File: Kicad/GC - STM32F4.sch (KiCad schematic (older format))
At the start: 16 parts, among them J2 SWD, U1 STM32F405RGT6, Y2 8MHz

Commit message: Passives changed from 0805 to 0603
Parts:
- C10, C11, C12, C13, C14, C15, C16, C17, C18, C19, C20, C9: footprint Capacitors_SMD:C_0805 -> Capacitors_SMD:C_0603
- R6: footprint Resistors_SMD:R_0805 -> Resistors_SMD:R_0603
- renumbered J2 to J9
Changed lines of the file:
@@
 F 0 "C11" H 7350 6300 50  0000 L CNN
 F 1 "2.2uF" H 7350 6100 50  0000 L CNN
-F 2 "Capacitors_SMD:C_0805" H 7300 6200 60  0001 C CNN
+F 2 "Capacitors_SMD:C_0603" H 7300 6200 60  0001 C CNN
 F 3 "" H 7300 6200 60  0001 C CNN
 	1    7300 6200
@@
 F 0 "C10" H 7350 6050 50  0000 L CNN
 F 1 "2.2uF" H 7350 5850 50  0000 L CNN
-F 2 "Capacitors_SMD:C_0805" H 7300 5950 60  0001 C CNN
+F 2 "Capacitors_SMD:C_0603" H 7300 5950 60  0001 C CNN
 F 3 "" H 7300 5950 60  0001 C CNN
 	1    7300 5950
@@
 F 0 "C9" H 7850 1800 50  0000 L CNN
 F 1 "15pF" H 8050 1800 50  0000 L CNN
-F 2 "Capacitors_SMD:C_0805" H 8000 1700 60  0001 C CNN
+F 2 "Capacitors_SMD:C_0603" H 8000 1700 60  0001 C CNN
 F 3 "" H 8000 1700 60  0001 C CNN
 	1    8000 1700
@@
 F 0 "C15" H 7800 1900 50  0000 L CNN
 F 1 "15pF" H 8050 1900 50  0000 L CNN
-F 2 "Capacitors_SMD:C_0805" H 8000 2000 60  0001 C CNN
+F 2 "Capacitors_SMD:C_0603" H 8000 2000 60  0001 C CNN
 F 3 "" H 8000 2000 60  0001 C CNN
 	1    8000 2000
@@
 F 0 "C12" H 7550 5650 50  0000 L CNN
 F 1 "2.2uF" H 7550 5450 50  0000 L CNN
-F 2 "Capacitors_SMD:C_0805" H 7500 5550 60  0001 C CNN
+F 2 "Capacitors_SMD:C_0603" H 7500 5550 60  0001 C CNN
 F 3 "" H 7500 5550 60  0001 C CNN
 	1    7500 5550
@@
 F 0 "C14" H 7800 5650 50  0000 L CNN
 F 1 "2.2uF" H 7800 5450 50  0000 L CNN
-F 2 "Capacitors_SMD:C_0805" H 7750 5550 60  0001 C CNN
+F 2 "Capacitors_SMD:C_0603" H 7750 5550 60  0001 C CNN
 F 3 "" H 7750 5550 60  0001 C CNN
 	1    7750 5550
@@
 F 0 "C13" H 7800 3050 50  0000 L CNN
 F 1 "100nF" H 7800 2850 50  0000 L CNN
-F 2 "Capacitors_SMD:C_0805" H 7750 2950 60  0001 C CNN
+F 2 "Capacitors_SMD:C_0603" H 7750 2950 60  0001 C CNN
 F 3 "" H 7750 2950 60  0001 C CNN
 	1    7750 2950
@@
 F 0 "C16" H 9450 1400 50  0000 L CNN
 F 1 "2.2uF" H 9450 1200 50  0000 L CNN
-F 2 "Capacitors_SMD:C_0805" H 9400 1300 60  0001 C CNN
+F 2 "Capacitors_SMD:C_0603" H 9400 1300 60  0001 C CNN
 F 3 "" H 9400 1300 60  0001 C CNN
 	1    9400 1300
@@
 F 0 "C17" H 9700 1400 50  0000 L CNN
 F 1 "2.2uF" H 9700 1200 50  0000 L CNN
-F 2 "Capacitors_SMD:C_0805" H 9650 1300 60  0001 C CNN
+F 2 "Capacitors_SMD:C_0603" H 9650 1300 60  0001 C CNN
 F 3 "" H 9650 1300 60  0001 C CNN
 	1    9650 1300
@@
 F 0 "C20" H 10450 1400 50  0000 L CNN
 F 1 "2.2uF" H 10450 1200 50  0000 L CNN
-F 2 "Capacitors_SMD:C_0805" H 10400 1300 60  0001 C CNN
+F 2 "Capacitors_SMD:C_0603" H 10400 1300 60  0001 C CNN
 F 3 "" H 10400 1300 60  0001 C CNN
 	1    10400 1300
@@
 F 0 "C18" H 9950 1400 50  0000 L CNN
 F 1 "2.2uF" H 9950 1200 50  0000 L CNN
-F 2 "Capacitors_SMD:C_0805" H 9900 1300 60  0001 C CNN
+F 2 "Capacitors_SMD:C_0603" H 9900 1300 60  0001 C CNN
 F 3 "" H 9900 1300 60  0001 C CNN
 	1    9900 1300
@@
 F 0 "C19" H 10200 1400 50  0000 L CNN
 F 1 "2.2uF" H 10200 1200 50  0000 L CNN
-F 2 "Capacitors_SMD:C_0805" H 10150 1300 60  0001 C CNN
+F 2 "Capacitors_SMD:C_0603" H 10150 1300 60  0001 C CNN
 F 3 "" H 10150 1300 60  0001 C CNN
 	1    10150 1300
@@
 	10150 1050 10400 1050
 $Comp
-L conn:Conn_02x03_Odd_Even J2
+L conn:Conn_02x03_Odd_Even J9
 U 1 1 53F77410
 P 9750 3050
-F 0 "J2" H 9800 3250 50  0000 C CNN
+F 0 "J9" H 9800 3250 50  0000 C CNN
 F 1 "SWD" H 9800 2850 50  0000 C CNN
 F 2 "Connectors:Tag-Connect_TC2030-IDC-NL" H 9750 3050 50  0001 C CNN
@@
 F 0 "R6" V 7350 2350 50  0000 C CNN
 F 1 "10k" V 7250 2350 50  0000 C CNN
-F 2 "Resistors_SMD:R_0805" V 7180 2350 50  0001 C CNN
+F 2 "Resistors_SMD:R_0603" V 7180 2350 50  0001 C CNN
 F 3 "" H 7250 2350 50  0001 C CNN
 	1    7250 2350

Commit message: Components placed
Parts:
- C12, C14, C16, C17, C18, C19, C20: value 2.2uF -> 100nF
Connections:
- net LAMP_CMD: now reaches U1.11 (PC3(ADC123_IN13))
- no-connect marks 9 -> 8
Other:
- moved on the sheet: C17, C18, C19, C20
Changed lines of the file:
@@
 $EndComp
 $Comp
-L Device:C C11
-U 1 1 53F757AE
-P 7300 6200
-AR Path="/53F757AE" Ref="C11"  Part="1"
-AR Path="/53F7501A/53F757AE" Ref="C11"  Part="1"
-F 0 "C11" H 7350 6300 50  0000 L CNN
-F 1 "2.2uF" H 7350 6100 50  0000 L CNN
-F 2 "Capacitors_SMD:C_0603" H 7300 6200 60  0001 C CNN
-F 3 "" H 7300 6200 60  0001 C CNN
-	1    7300 6200
-	0    -1   1    0
-$EndComp
-$Comp
-L Device:C C10
-U 1 1 53F757B5
-P 7300 5950
-AR Path="/53F757B5" Ref="C10"  Part="1"
-AR Path="/53F7501A/53F757B5" Ref="C10"  Part="1"
-F 0 "C10" H 7350 6050 50  0000 L CNN
-F 1 "2.2uF" H 7350 5850 50  0000 L CNN
-F 2 "Capacitors_SMD:C_0603" H 7300 5950 60  0001 C CNN
-F 3 "" H 7300 5950 60  0001 C CNN
-	1    7300 5950
-	0    -1   -1   0
-$EndComp
-$Comp
 L Device:C C9
 U 1 1 53F757DB
@@
 AR Path="/53F7501A/53F757F8" Ref="C12"  Part="1"
 F 0 "C12" H 7550 5650 50  0000 L CNN
-F 1 "2.2uF" H 7550 5450 50  0000 L CNN
+F 1 "100nF" H 7550 5450 50  0000 L CNN
 F 2 "Capacitors_SMD:C_0603" H 7500 5550 60  0001 C CNN
 F 3 "" H 7500 5550 60  0001 C CNN
@@
 AR Path="/53F7501A/53F757FF" Ref="C14"  Part="1"
 F 0 "C14" H 7800 5650 50  0000 L CNN
-F 1 "2.2uF" H 7800 5450 50  0000 L CNN
+F 1 "100nF" H 7800 5450 50  0000 L CNN
 F 2 "Capacitors_SMD:C_0603" H 7750 5550 60  0001 C CNN
 F 3 "" H 7750 5550 60  0001 C CNN
@@
 $EndComp
 NoConn ~ 7000 3300
-NoConn ~ 4500 4850
 Text GLabel 10050 3050 2    60   Input ~ 0
 SWCLK
@@
 AR Path="/53F7501A/53F77426" Ref="C16"  Part="1"
 F 0 "C16" H 9450 1400 50  0000 L CNN
-F 1 "2.2uF" H 9450 1200 50  0000 L CNN
+F 1 "100nF" H 9450 1200 50  0000 L CNN
 F 2 "Capacitors_SMD:C_0603" H 9400 1300 60  0001 C CNN
 F 3 "" H 9400 1300 60  0001 C CNN
@@
 L Device:C C17
 U 1 1 53F7742D
-P 9650 1300
+P 9700 1300
 AR Path="/53F7742D" Ref="C17"  Part="1"
 AR Path="/53F7501A/53F7742D" Ref="C17"  Part="1"
-F 0 "C17" H 9700 1400 50  0000 L CNN
-F 1 "2.2uF" H 9700 1200 50  0000 L CNN
-F 2 "Capacitors_SMD:C_0603" H 9650 1300 60  0001 C CNN
-F 3 "" H 9650 1300 60  0001 C CNN
-	1    9650 1300
+F 0 "C17" H 9750 1400 50  0000 L CNN
+F 1 "100nF" H 9750 1200 50  0000 L CNN
+F 2 "Capacitors_SMD:C_0603" H 9700 1300 60  0001 C CNN
+F 3 "" H 9700 1300 60  0001 C CNN
+	1    9700 1300
 	-1   0    0    1
 $EndComp
@@
 L Device:C C20
 U 1 1 53F77434
-P 10400 1300
+P 10650 1300
 AR Path="/53F77434" Ref="C20"  Part="1"
 AR Path="/53F7501A/53F77434" Ref="C20"  Part="1"
-F 0 "C20" H 10450 1400 50  0000 L CNN
-F 1 "2.2uF" H 10450 1200 50  0000 L CNN
-F 2 "Capacitors_SMD:C_0603" H 10400 1300 60  0001 C CNN
-F 3 "" H 10400 1300 60  0001 C CNN
-	1    10400 1300
+F 0 "C20" H 10700 1400 50  0000 L CNN
+F 1 "100nF" H 10700 1200 50  0000 L CNN
+F 2 "Capacitors_SMD:C_0603" H 10650 1300 60  0001 C CNN
+F 3 "" H 10650 1300 60  0001 C CNN
+	1    10650 1300
 	-1   0    0    1
 $EndComp
@@
 L Device:C C18
 U 1 1 53F77447
-P 9900 1300
+P 10000 1300
 AR Path="/53F77447" Ref="C18"  Part="1"
 AR Path="/53F7501A/53F77447" Ref="C18"  Part="1"
-F 0 "C18" H 9950 1400 50  0000 L CNN
-F 1 "2.2uF" H 9950 1200 50  0000 L CNN
-F 2 "Capacitors_SMD:C_0603" H 9900 1300 60  0001 C CNN
-F 3 "" H 9900 1300 60  0001 C CNN
-	1    9900 1300
+F 0 "C18" H 10050 1400 50  0000 L CNN
+F 1 "100nF" H 10050 1200 50  0000 L CNN
+F 2 "Capacitors_SMD:C_0603" H 10000 1300 60  0001 C CNN
+F 3 "" H 10000 1300 60  0001 C CNN
+	1    10000 1300
 	-1   0    0    1
 $EndComp
@@
 L Device:C C19
 U 1 1 53F7744E
-P 10150 1300
+P 10350 1300
 AR Path="/53F7744E" Ref="C19"  Part="1"
 AR Path="/53F7501A/53F7744E" Ref="C19"  Part="1"
-F 0 "C19" H 10200 1400 50  0000 L CNN
-F 1 "2.2uF" H 10200 1200 50  0000 L CNN
-F 2 "Capacitors_SMD:C_0603" H 10150 1300 60  0001 C CNN
-F 3 "" H 10150 1300 60  0001 C CNN
-	1    10150 1300
+F 0 "C19" H 10400 1400 50  0000 L CNN
+F 1 "100nF" H 10400 1200 50  0000 L CNN
+F 2 "Capacitors_SMD:C_0603" H 10350 1300 60  0001 C CNN
+F 3 "" H 10350 1300 60  0001 C CNN
+	1    10350 1300
 	-1   0    0    1
 $EndComp
-Connection ~ 10150 1550
 Wire Wire Line
-	10150 1550 10150 1450
-Connection ~ 9900 1550
+	10350 1550 10350 1450
 Wire Wire Line
-	9900 1550 9900 1450
-Connection ~ 9650 1550
+	10000 1550 10000 1450
 Wire Wire Line
-	9650 1550 9650 1450
-Connection ~ 9400 1550
+	9700 1550 9700 1450
 Wire Wire Line
 	9400 1450 9400 1550
-Connection ~ 9400 1050
 Wire Wire Line
 	9400 1050 9400 1150
-Connection ~ 9650 1050
 Wire Wire Line
-	9650 1050 9650 1150
-Connection ~ 9900 1050
+	9700 1050 9700 1150
 Wire Wire Line
-	9900 1050 9900 1150
-Connection ~ 10150 1050
+	10000 1050 10000 1150
 Wire Wire Line
-	10150 1050 10150 1150
+	10350 1050 10350 1150
 Wire Wire Line
-	10400 1050 10400 1150
+	10650 1050 10650 1150
 Wire Wire Line
 	9100 1050 9400 1050
@@
 	9100 1000 9100 1050
 Wire Wire Line
-	10400 1550 10400 1450
+	10650 1550 10650 1450
 Wire Wire Line
 	9100 1550 9400 1550
@@
 EndData
 $EndBitmap
-Text Notes 9300 1650 0    40   ~ 0
+Text Notes 9500 1650 0    40   ~ 0
 Bypass, place next to VDD pins
 Text HLabel 4500 3650 0    60   Input ~ 0
@@
 Wire Wire Line
 	7500 5950 7500 6200
-Wire Wire Line
-	10150 1550 10400 1550
-Wire Wire Line
-	9900 1550 10150 1550
-Wire Wire Line
-	9650 1550 9900 1550
-Wire Wire Line
-	9400 1550 9650 1550
-Wire Wire Line
-	9400 1050 9650 1050
-Wire Wire Line
-	9650 1050 9900 1050
-Wire Wire Line
-	9900 1050 10150 1050
-Wire Wire Line
-	10150 1050 10400 1050
 $Comp
 L conn:Conn_02x03_Odd_Even J9
@@
 Text HLabel 4500 5450 0    60   Input ~ 0
 BRAKE
+Wire Wire Line
+	9400 1550 9700 1550
+Connection ~ 9400 1550
+Connection ~ 9700 1550
+Wire Wire Line
+	9700 1550 10000 1550
+Connection ~ 10000 1550
+Wire Wire Line
+	10000 1550 10350 1550
+Connection ~ 10350 1550
+Wire Wire Line
+	10350 1550 10650 1550
+Wire Wire Line
+	9400 1050 9700 1050
+Connection ~ 9400 1050
+Connection ~ 9700 1050
+Wire Wire Line
+	9700 1050 10000 1050
+Connection ~ 10000 1050
+Wire Wire Line
+	10000 1050 10350 1050
+Connection ~ 10350 1050
+Wire Wire Line
+	10350 1050 10650 1050
+$Comp
+L Device:C C11
+U 1 1 53F757AE
+P 7300 6200
+AR Path="/53F757AE" Ref="C11"  Part="1"
+AR Path="/53F7501A/53F757AE" Ref="C11"  Part="1"
+F 0 "C11" H 7350 6300 50  0000 L CNN
+F 1 "2.2uF" H 7350 6100 50  0000 L CNN
+F 2 "Capacitors_SMD:C_0603" H 7300 6200 60  0001 C CNN
+F 3 "" H 7300 6200 60  0001 C CNN
+	1    7300 6200
+	0    -1   1    0
+$EndComp
+$Comp
+L Device:C C10
+U 1 1 53F757B5
+P 7300 5950
+AR Path="/53F757B5" Ref="C10"  Part="1"
+AR Path="/53F7501A/53F757B5" Ref="C10"  Part="1"
+F 0 "C10" H 7350 6050 50  0000 L CNN
+F 1 "2.2uF" H 7350 5850 50  0000 L CNN
+F 2 "Capacitors_SMD:C_0603" H 7300 5950 60  0001 C CNN
+F 3 "" H 7300 5950 60  0001 C CNN
+	1    7300 5950
+	0    -1   -1   0
+$EndComp
+Text HLabel 4500 4850 0    60   Output ~ 0
+LAMP_CMD
 $EndSCHEMATC

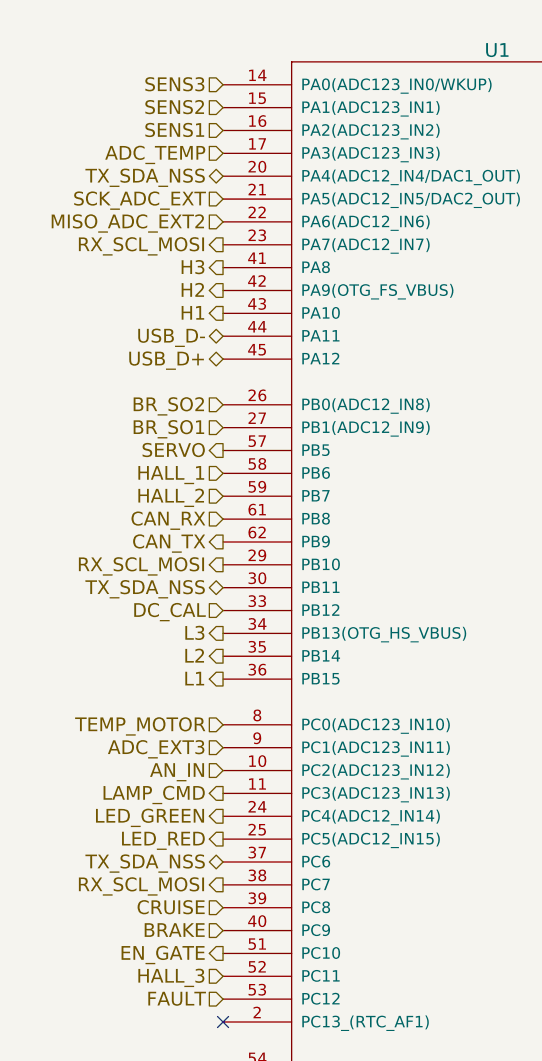
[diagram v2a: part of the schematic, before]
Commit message: Adjusting capacitor size/value
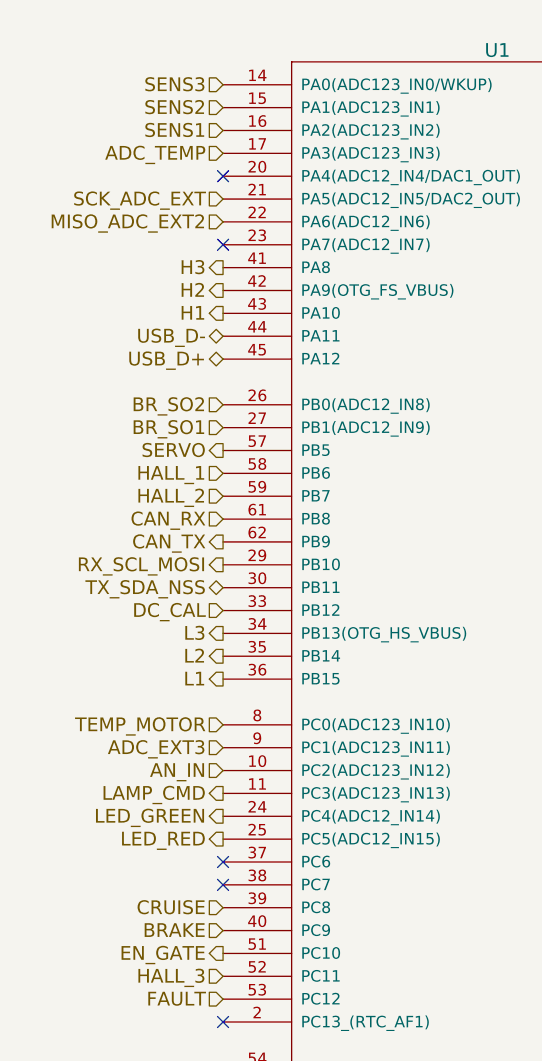
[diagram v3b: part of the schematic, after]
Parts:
- C10, C11: Tension (none) -> 25V
- C12, C13, C14, C15, C16, C17, C18, C19, C20, C9: Tension (none) -> 50V
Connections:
- net RX_SCL_MOSI: no longer U1.23 (PA7(ADC12_IN7)), U1.38 (PC7)
- net TX_SDA_NSS: no longer U1.20 (PA4(ADC12_IN4/DAC1_OUT)), U1.37 (PC6)
- no-connect marks 8 -> 12
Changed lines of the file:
@@
 F 2 "Capacitors_SMD:C_0603" H 8000 1700 60  0001 C CNN
 F 3 "" H 8000 1700 60  0001 C CNN
+F 4 "50V" H 8000 1700 50  0001 C CNN "Tension"
 	1    8000 1700
 	1    0    0    -1
@@
 F 2 "Capacitors_SMD:C_0603" H 8000 2000 60  0001 C CNN
 F 3 "" H 8000 2000 60  0001 C CNN
+F 4 "50V" H 8000 2000 50  0001 C CNN "Tension"
 	1    8000 2000
 	1    0    0    -1
@@
 F 2 "Capacitors_SMD:C_0603" H 7500 5550 60  0001 C CNN
 F 3 "" H 7500 5550 60  0001 C CNN
+F 4 "50V" H 7500 5550 50  0001 C CNN "Tension"
 	1    7500 5550
 	-1   0    0    1
@@
 F 2 "Capacitors_SMD:C_0603" H 7750 5550 60  0001 C CNN
 F 3 "" H 7750 5550 60  0001 C CNN
+F 4 "50V" H 7750 5550 50  0001 C CNN "Tension"
 	1    7750 5550
 	1    0    0    1
@@
 F 2 "Capacitors_SMD:C_0603" H 7750 2950 60  0001 C CNN
 F 3 "" H 7750 2950 60  0001 C CNN
+F 4 "50V" H 7750 2950 50  0001 C CNN "Tension"
 	1    7750 2950
 	-1   0    0    1
@@
 F 2 "Capacitors_SMD:C_0603" H 9400 1300 60  0001 C CNN
 F 3 "" H 9400 1300 60  0001 C CNN
+F 4 "50V" H 9400 1300 50  0001 C CNN "Tension"
 	1    9400 1300
 	-1   0    0    1
@@
 F 2 "Capacitors_SMD:C_0603" H 9700 1300 60  0001 C CNN
 F 3 "" H 9700 1300 60  0001 C CNN
+F 4 "50V" H 9700 1300 50  0001 C CNN "Tension"
 	1    9700 1300
 	-1   0    0    1
@@
 F 2 "Capacitors_SMD:C_0603" H 10650 1300 60  0001 C CNN
 F 3 "" H 10650 1300 60  0001 C CNN
+F 4 "50V" H 10650 1300 50  0001 C CNN "Tension"
 	1    10650 1300
 	-1   0    0    1
@@
 F 2 "Capacitors_SMD:C_0603" H 10000 1300 60  0001 C CNN
 F 3 "" H 10000 1300 60  0001 C CNN
+F 4 "50V" H 10000 1300 50  0001 C CNN "Tension"
 	1    10000 1300
 	-1   0    0    1
@@
 F 2 "Capacitors_SMD:C_0603" H 10350 1300 60  0001 C CNN
 F 3 "" H 10350 1300 60  0001 C CNN
+F 4 "50V" H 10350 1300 50  0001 C CNN "Tension"
 	1    10350 1300
 	-1   0    0    1
@@
 Text HLabel 4500 2250 0    60   Input ~ 0
 SCK_ADC_EXT
-Text HLabel 4500 5150 0    60   3State ~ 0
-TX_SDA_NSS
-Text HLabel 4500 5250 0    60   Output ~ 0
-RX_SCL_MOSI
 Text HLabel 4500 5750 0    60   Input ~ 0
 FAULT
@@
 Text HLabel 4500 2350 0    60   Input ~ 0
 MISO_ADC_EXT2
-Text HLabel 4500 2450 0    60   Output ~ 0
-RX_SCL_MOSI
 Text HLabel 4500 2050 0    60   Input ~ 0
 ADC_TEMP
-Text HLabel 4500 2150 0    60   3State ~ 0
-TX_SDA_NSS
 Wire Wire Line
 	7750 5750 7750 5800
@@
 F 2 "Capacitors_SMD:C_0603" H 7300 6200 60  0001 C CNN
 F 3 "" H 7300 6200 60  0001 C CNN
+F 4 "25V" H 7300 6200 50  0001 C CNN "Tension"
 	1    7300 6200
 	0    -1   1    0
@@
 F 2 "Capacitors_SMD:C_0603" H 7300 5950 60  0001 C CNN
 F 3 "" H 7300 5950 60  0001 C CNN
+F 4 "25V" H 7300 5950 50  0001 C CNN "Tension"
 	1    7300 5950
 	0    -1   -1   0
@@
 Text HLabel 4500 4850 0    60   Output ~ 0
 LAMP_CMD
+NoConn ~ 4500 5250
+NoConn ~ 4500 5150
+NoConn ~ 4500 2450
+NoConn ~ 4500 2150
 $EndSCHEMATC
